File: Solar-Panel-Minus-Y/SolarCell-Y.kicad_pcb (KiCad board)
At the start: 6 copper layers, 64 x 58 mm, 67 parts, among them IC2 TSL2561, J1 XF2M-1015-1A, J3 BATTERY CONNECTOR, J4 B2B-PH-SM4-TB_LF__SN_, U2 Value, U3 SW_SPDT, U4 SW_SPDT

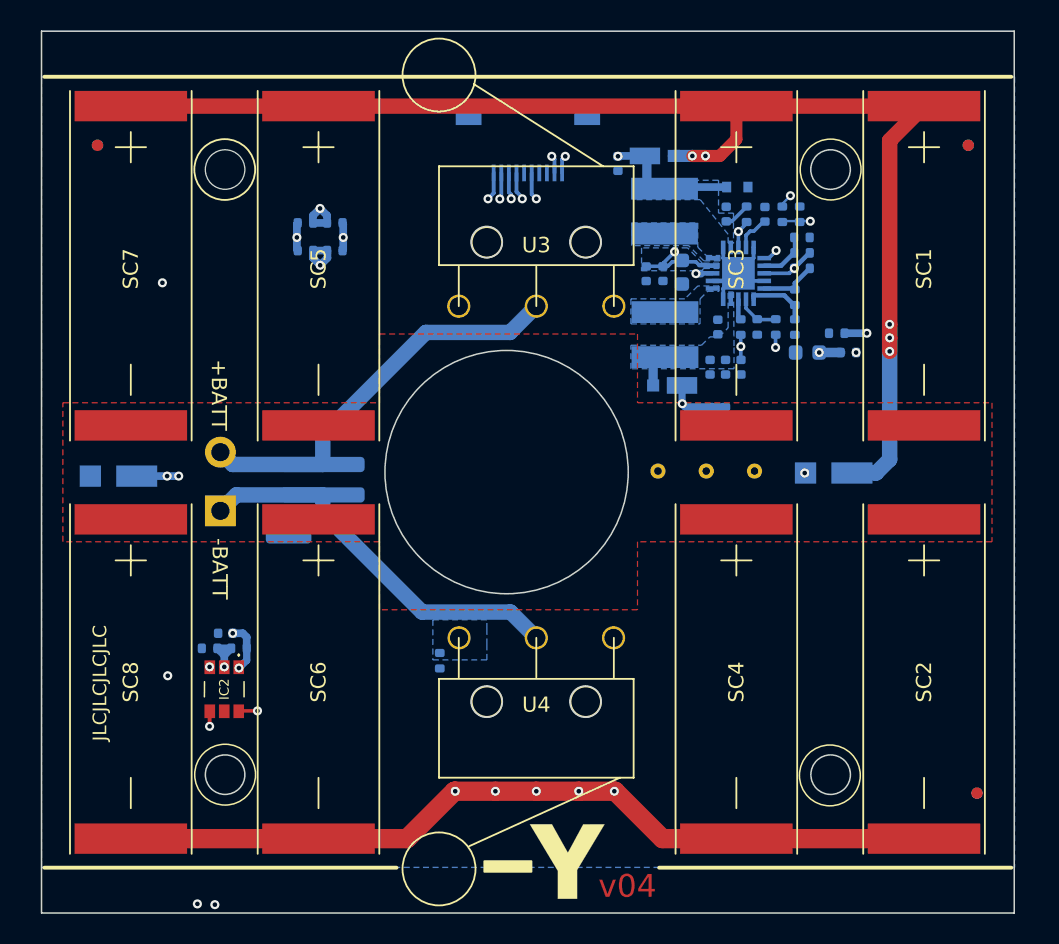
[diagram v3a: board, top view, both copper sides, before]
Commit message: Added JLC order number silkscreen
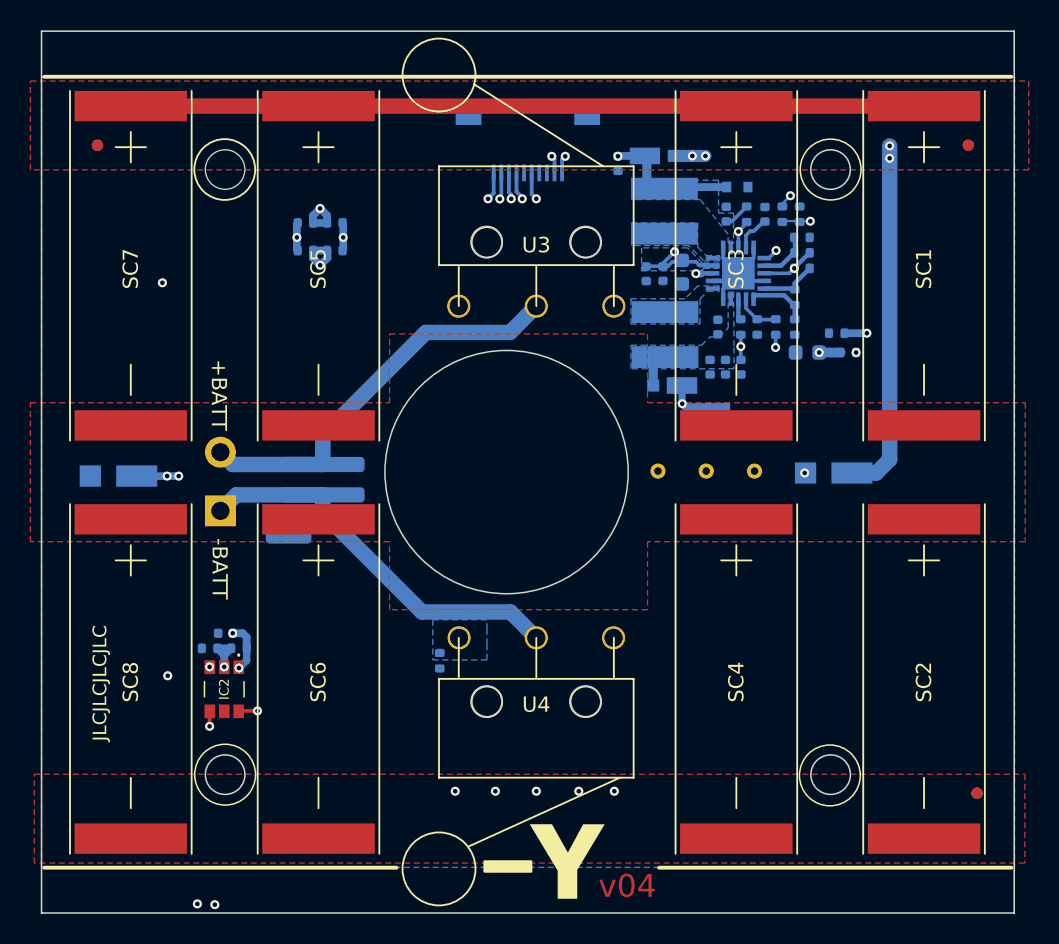
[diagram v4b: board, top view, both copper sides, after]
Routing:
- net GND: track 64.2 -> 9.43 mm
- net /VSOLAR_FULL: track 88.6 -> 77.7 mm, vias 5 -> 4
- added copper zone on F.Cu, net /VSOLAR_FULL
- added copper zone on F.Cu, net GND
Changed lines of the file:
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@@
   (via (at 163.195 99.06) (size 0.6) (drill 0.3) (layers "F.Cu" "B.Cu") (net 1))
   (segment (start 119.2592 99.2632) (end 122.0216 99.2632) (width 0.508) (layer "B.Cu") (net 1))
-  (segment (start 142.8496 119.9896) (end 145.542 119.9896) (width 1.27) (layer "F.Cu") (net 2))
-  (segment (start 140.208 119.9896) (end 142.8496 119.9896) (width 1.27) (layer "F.Cu") (net 2))
-  (segment (start 148.336 119.9896) (end 150.6728 119.9896) (width 1.27) (layer "F.Cu") (net 2))
-  (segment (start 150.7236 119.9896) (end 153.842 123.108) (width 1.27) (layer "F.Cu") (net 2))
-  (segment (start 171.0436 123.108) (end 158.6992 123.108) (width 1.27) (layer "F.Cu") (net 2))
-  (segment (start 137.0388 123.108) (end 140.1572 119.9896) (width 1.27) (layer "F.Cu") (net 2))
-  (segment (start 150.6728 119.9896) (end 150.7236 119.9896) (width 1.27) (layer "F.Cu") (net 2))
-  (segment (start 118.872 123.108) (end 131.2164 123.108) (width 1.27) (layer "F.Cu") (net 2))
-  (segment (start 131.2164 123.108) (end 137.0388 123.108) (width 1.27) (layer "F.Cu") (net 2))
-  (segment (start 145.542 119.9896) (end 148.336 119.9896) (width 1.27) (layer "F.Cu") (net 2))
-  (segment (start 153.842 123.108) (end 158.6992 123.108) (width 1.27) (layer "F.Cu") (net 2))
-  (segment (start 140.1572 119.9896) (end 140.208 119.9896) (width 1.27) (layer "F.Cu") (net 2))
   (via (at 140.208 119.9896) (size 0.6) (drill 0.3) (layers "F.Cu" "B.Cu") (net 2))
   (via (at 148.336 119.9896) (size 0.6) (drill 0.3) (layers "F.Cu" "B.Cu") (net 2))
@@
   (segment (start 153.2285 93.14224) (end 153.2285 91.26804) (width 0.6096) (layer "B.Cu") (net 27))
   (segment (start 153.2285 91.26804) (end 153.272 91.22454) (width 0.6096) (layer "B.Cu") (net 27))
-  (segment (start 168.783 89.281) (end 168.783 90.17) (width 1.016) (layer "F.Cu") (net 28))
   (segment (start 158.6992 74.93) (end 131.2164 74.93) (width 1.016) (layer "F.Cu") (net 28))
-  (segment (start 168.783 89.281) (end 168.783 77.1906) (width 1.016) (layer "F.Cu") (net 28))
-  (segment (start 157.605705 78.207895) (end 158.6992 77.1144) (width 0.8) (layer "F.Cu") (net 28))
   (segment (start 171.0436 74.93) (end 158.6992 74.93) (width 1.016) (layer "F.Cu") (net 28))
   (segment (start 131.2164 74.93) (end 118.872 74.93) (width 1.016) (layer "F.Cu") (net 28))
-  (segment (start 168.783 77.1906) (end 171.0436 74.93) (width 1.016) (layer "F.Cu") (net 28))
-  (segment (start 158.6992 77.1144) (end 158.6992 74.93) (width 0.8) (layer "F.Cu") (net 28))
-  (segment (start 155.803703 78.207895) (end 157.605705 78.207895) (width 0.8) (layer "F.Cu") (net 28))
-  (segment (start 168.783 90.17) (end 168.783 91.059) (width 1.016) (layer "F.Cu") (net 28))
-  (via (at 168.783 89.281) (size 0.6) (drill 0.3) (layers "F.Cu" "B.Cu") (net 28))
+  (via (at 168.783 77.5485) (size 0.6) (drill 0.3) (layers "F.Cu" "B.Cu") (net 28))
   (via (at 156.666833 78.207895) (size 0.6) (drill 0.3) (layers "F.Cu" "B.Cu") (net 28))
-  (via (at 168.783 90.17) (size 0.6) (drill 0.3) (layers "F.Cu" "B.Cu") (net 28))
+  (via (at 168.783 78.359) (size 0.6) (drill 0.3) (layers "F.Cu" "B.Cu") (net 28))
   (via (at 155.803703 78.207895) (size 0.6) (drill 0.3) (layers "F.Cu" "B.Cu") (net 28))
-  (via (at 168.783 91.059) (size 0.6) (drill 0.3) (layers "F.Cu" "B.Cu") (net 28))
   (segment (start 155.803703 78.207895) (end 156.666833 78.207895) (width 0.8) (layer "B.Cu") (net 28))
+  (segment (start 167.894 99.06) (end 166.3 99.06) (width 1.016) (layer "B.Cu") (net 28))
+  (segment (start 155.801548 78.20574) (end 155.803703 78.207895) (width 0.8) (layer "B.Cu") (net 28))
+  (segment (start 168.783 77.5485) (end 168.783 98.171) (width 1.016) (layer "B.Cu") (net 28))
+  (segment (start 154.5855 78.20574) (end 155.801548 78.20574) (width 0.8) (layer "B.Cu") (net 28))
   (segment (start 168.783 98.171) (end 167.894 99.06) (width 1.016) (layer "B.Cu") (net 28))
-  (segment (start 155.801548 78.20574) (end 155.803703 78.207895) (width 0.8) (layer "B.Cu") (net 28))
-  (segment (start 168.783 89.281) (end 168.783 98.171) (width 1.016) (layer "B.Cu") (net 28))
-  (segment (start 154.5855 78.20574) (end 155.801548 78.20574) (width 0.8) (layer "B.Cu") (net 28))
-  (segment (start 167.894 99.06) (end 166.3 99.06) (width 1.016) (layer "B.Cu") (net 28))
   (segment (start 160.062 88.97074) (end 161.2775 88.97074) (width 0.24) (layer "B.Cu") (net 29))
   (segment (start 159.332844 87.6264) (end 159.332844 88.226084) (width 0.2286) (layer "B.Cu") (net 29))
   (segment (start 159.332844 88.226084) (end 160.003 88.89624) (width 0.2286) (layer "B.Cu") (net 29))
+  (zone (net 2) (net_name "GND") (layer "F.Cu") (hatch edge 0.508)
+    (connect_pads (clearance 0))
+    (min_thickness 0.254) (filled_areas_thickness no)
+    (fill yes (thermal_gap 0.508) (thermal_bridge_width 0.508))
+    (polygon
+      (pts
+        (xy 177.673 124.714)
+        (xy 112.522 124.714)
+        (xy 112.522 118.872)
+        (xy 177.673 118.872)
+      )
+    )
+  )
   (zone (net 0) (net_name "") (layers F&B.Cu) (hatch edge 0.508)
     (connect_pads (clearance 0))
@@
     )
   )
+  (zone (net 28) (net_name "/VSOLAR_FULL") (layer "F.Cu") (hatch edge 0.508)
+    (connect_pads (clearance 0))
+    (min_thickness 0.254) (filled_areas_thickness no)
+    (fill yes (thermal_gap 0.508) (thermal_bridge_width 0.508))
+    (polygon
+      (pts
+        (xy 177.927 79.121)
+        (xy 112.268 79.121)
+        (xy 112.268 73.279)
+        (xy 177.927 73.279)
+      )
+    )
+  )
   (zone (net 1) (net_name "Net-(D11-Pad2)") (layer "F.Cu") (hatch edge 0.508)
     (connect_pads (clearance 0.2032))
@@
     (polygon
       (pts
-        (xy 152.1968 94.4372)
-        (xy 175.514 94.4372)
-        (xy 175.514 103.5812)
-        (xy 152.1968 103.5812)
-        (xy 152.1968 108.0516)
-        (xy 135.2296 108.0516)
-        (xy 135.2296 103.5812)
-        (xy 114.4016 103.5812)
-        (xy 114.4016 94.4372)
-        (xy 135.2296 94.4372)
-        (xy 135.2296 89.916)
-        (xy 152.1968 89.916)
+        (xy 152.8572 94.4372)
+        (xy 177.6984 94.4372)
+        (xy 177.6984 103.5812)
+        (xy 152.8572 103.5812)
+        (xy 152.8572 108.0516)
+        (xy 135.89 108.0516)
+        (xy 135.89 103.5812)
+        (xy 112.268 103.5812)
+        (xy 112.268 94.4372)
+        (xy 135.89 94.4372)
+        (xy 135.89 89.916)
+        (xy 152.8572 89.916)
       )
     )

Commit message: Made Requested Changes
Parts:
- moved Ref** 77.4 mm to (97.4, 82.7), turned to 180 degrees
- moved R14 76.4 mm to (97.8, 56.9), turned to 0 degrees
- moved R15 75.6 mm to (97.8, 55.8), turned to 0 degrees
- moved C6 71.0 mm to (101.9, 55.6), turned to 0 degrees
- moved D11 66.7 mm to (112.5, 58.0)
- moved IC2 58.7 mm to (125.2, 54.6)
- moved R17 58.1 mm to (116.6, 53.2), turned to 90 degrees
- moved C5 56.3 mm to (115.6, 54.1), turned to 90 degrees
- moved R18 56.0 mm to (116.6, 55.1), turned to 90 degrees
- moved J1 54.9 mm to (96.1, 54.3), turned to 90 degrees
- moved R1000 54.8 mm to (99.1, 74.0), turned to 90 degrees
- moved REF** 53.0 mm to (134.4, 85.5) (x2)
- moved SC1 53.0 mm to (130.9, 40.4)
- moved SC2 53.0 mm to (130.9, 67.5)
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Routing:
- net BATT_P: track 40.5 -> 5.94 mm, vias 2 -> 1
- net BATT_N: track 31.5 -> 1.31 mm, vias 2 -> 0
- net SCL1: track 54.0 -> 31.4 mm
- net VSOLAR: track 34.7 -> 12.4 mm, vias 1 -> 0
- net Net-(J3-Pad2): track 26.5 -> 48.3 mm
- net /VBAT: track 12.7 -> 32.2 mm
- net SDA1: track 49.6 -> 33.9 mm
- net Net-(IC2-Pad2): track 2.96 -> 11.6 mm, vias 1 -> 2
- net Net-(C10-Pad1): track 15.8 -> 7.45 mm
- net Net-(J3-Pad1): track 25.8 -> 33.8 mm
- net COIL_P: track 23.6 -> 31.5 mm
- net Net-(R11-Pad1): track 8.95 -> 3.78 mm, vias 2 -> 0
- net COIL_N: track 21.9 -> 26.8 mm
- net Net-(D11-Pad2): track 5.25 -> 2.48 mm, vias 3 -> 4
- net /VSOLAR_FULL: track 77.7 -> 79.9 mm, vias 4 -> 5
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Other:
- rule pad_to_mask_clearance: 0.049 -> 0.0508

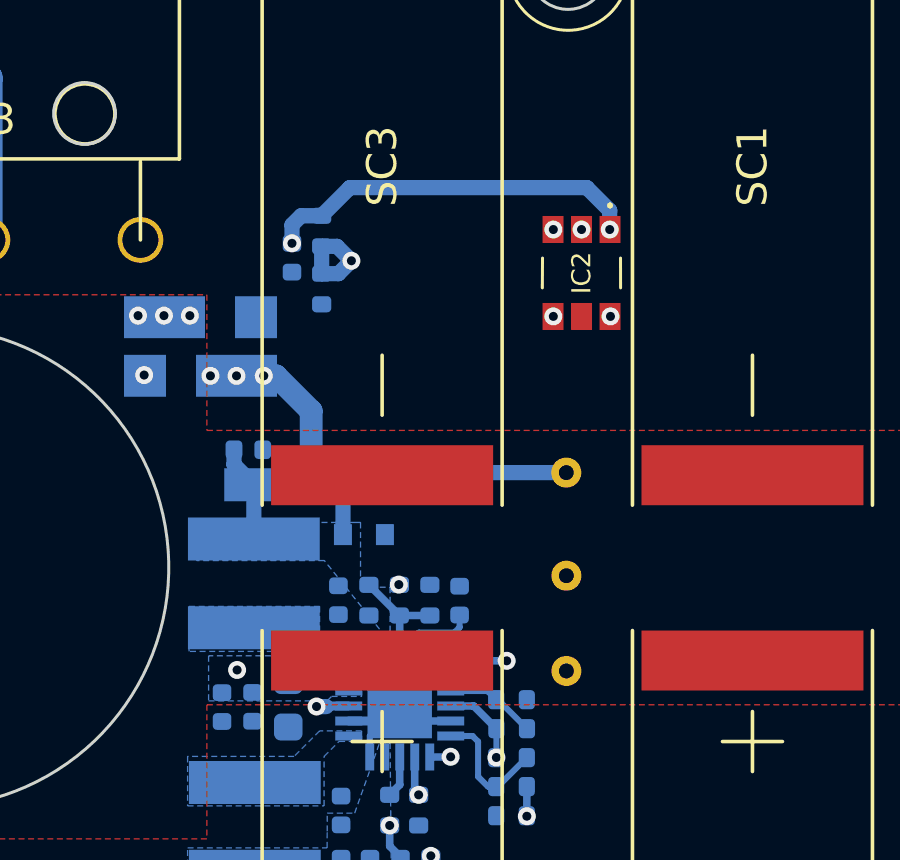
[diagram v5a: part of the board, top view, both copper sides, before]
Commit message: Done with X, +/-Y, and +Z. TODO: -Z
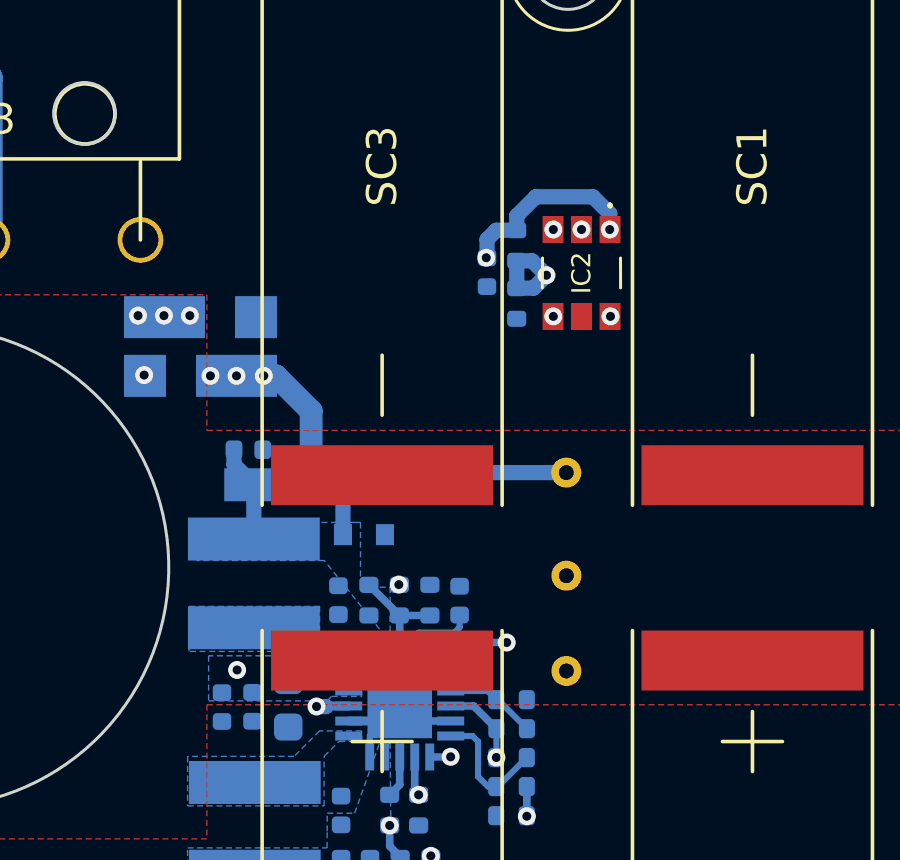
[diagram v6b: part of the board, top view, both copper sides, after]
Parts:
- moved C5 6.52 mm to (122.1, 54.6)
- moved R17 6.52 mm to (123.1, 53.7)
- moved R18 6.52 mm to (123.1, 55.6)
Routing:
- net Net-(IC2-Pad2): track 11.6 -> 5.69 mm
- net +3V3: track 72.5 -> 69.5 mm
- net VOUT_EN: track 11.7 -> 12.2 mm
